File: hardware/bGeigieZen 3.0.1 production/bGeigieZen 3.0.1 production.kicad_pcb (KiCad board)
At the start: 2 copper layers, 129.4 x 64.6 mm, 17 parts, among them J1 M5 2x15 pin, J10 QI GND, J11 QI charger Plus, J2 Geiger IRover, J3 GPS, J4 Geiger Safepulse, J5 Extra support header, J6 Grove, J8 QI charger ground, J9 QI Plus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

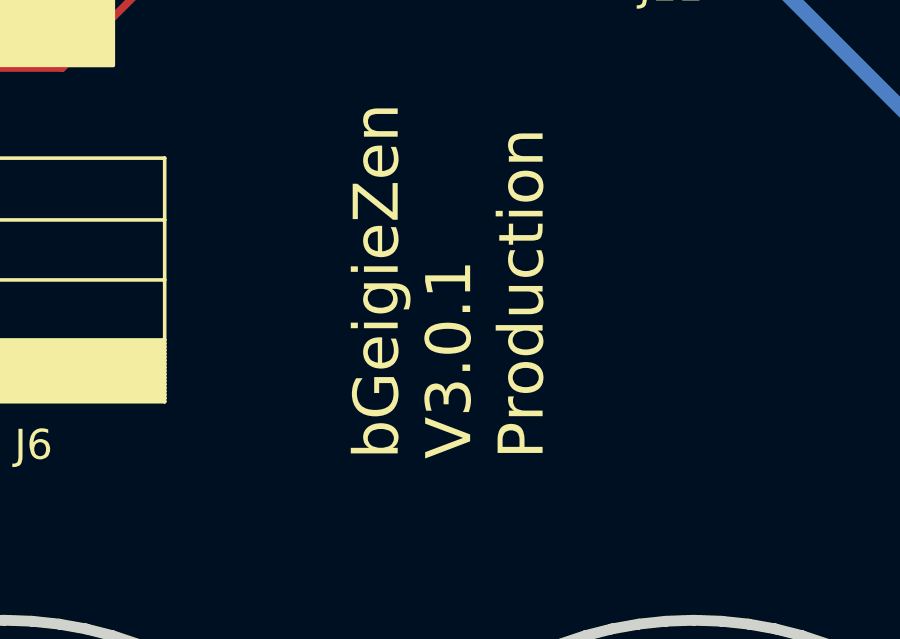
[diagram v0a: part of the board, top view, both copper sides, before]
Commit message: Updated text of version on board
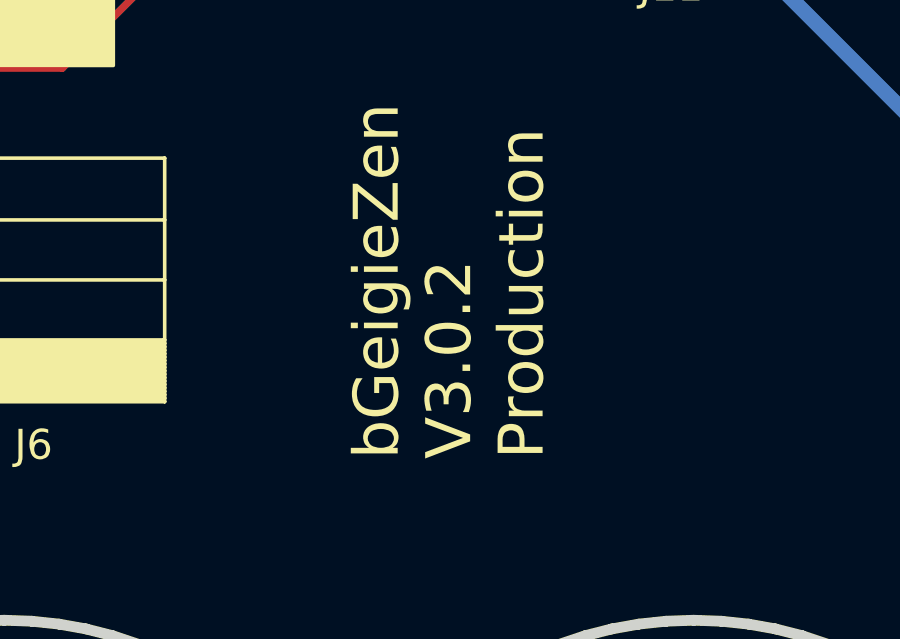
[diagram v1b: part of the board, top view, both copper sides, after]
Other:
- board text added: "bGeigieZen V3.0.2 Production"
- board text removed: "bGeigieZen V3.0.1 Production"
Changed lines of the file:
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@@
 		)
 	)
-	(gr_text "bGeigieZen\nV3.0.1  Production"
+	(gr_text "bGeigieZen\nV3.0.2  Production"
 		(at 102.7176 83.006 90)
 		(layer "B.SilkS")
@@
 		)
 	)
-	(gr_text "bGeigieZen \nV3.0.1\nProduction"
+	(gr_text "bGeigieZen \nV3.0.2\nProduction"
 		(at 175.6156 123.138 90)
 		(layer "F.SilkS")
